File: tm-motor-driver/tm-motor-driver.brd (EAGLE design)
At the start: 50 x 27 mm, 18 parts

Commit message: Generate gerber files
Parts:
- moved C1 2.12 mm to (23.5, 12.5)
- moved C2 2.12 mm to (26.9, 16.5)
- moved D_0 2.12 mm to (33.5, 17.5)
- moved D_1 2.12 mm to (13.5, 17.5)
- moved LED_0 2.12 mm to (30.5, 17.5)
- moved LED_1 2.12 mm to (16.5, 17.5)
- moved MOSFET_0 2.12 mm to (34.5, 12.5)
- moved MOSFET_1 2.12 mm to (12.5, 12.5)
- moved MOTOR_0 2.12 mm to (41.5, 16.5)
- moved MOTOR_1 2.12 mm to (5.50, 16.5)
- moved POWER 2.12 mm to (17.5, 5.50)
- moved PWM 2.12 mm to (29.5, 5.50)
- moved R1 2.12 mm to (29.5, 12.5)
- moved R2 2.12 mm to (30.5, 22.5)
- moved R3 2.12 mm to (17.5, 12.5)
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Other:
- board size 50 x 27 mm -> 47 x 26 mm

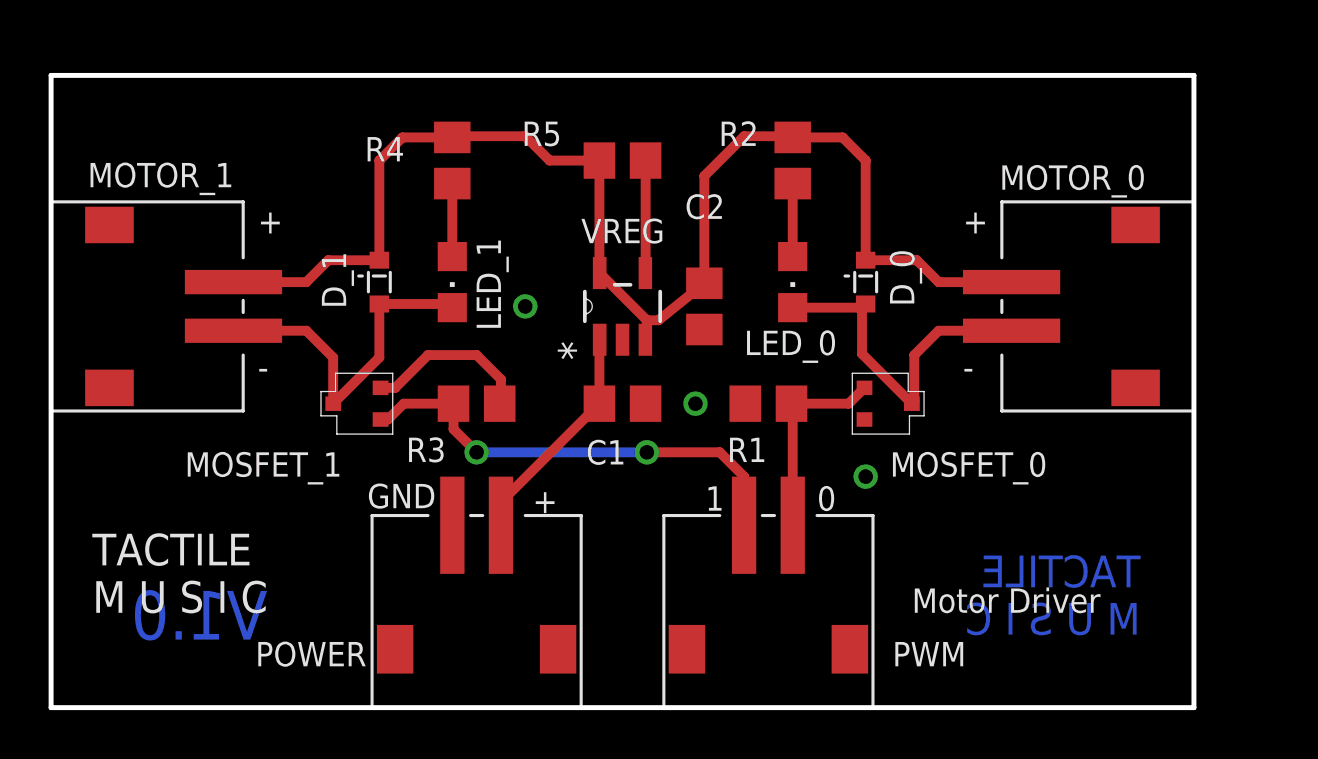
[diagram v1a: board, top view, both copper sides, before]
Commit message: Replaced JST with picoblade
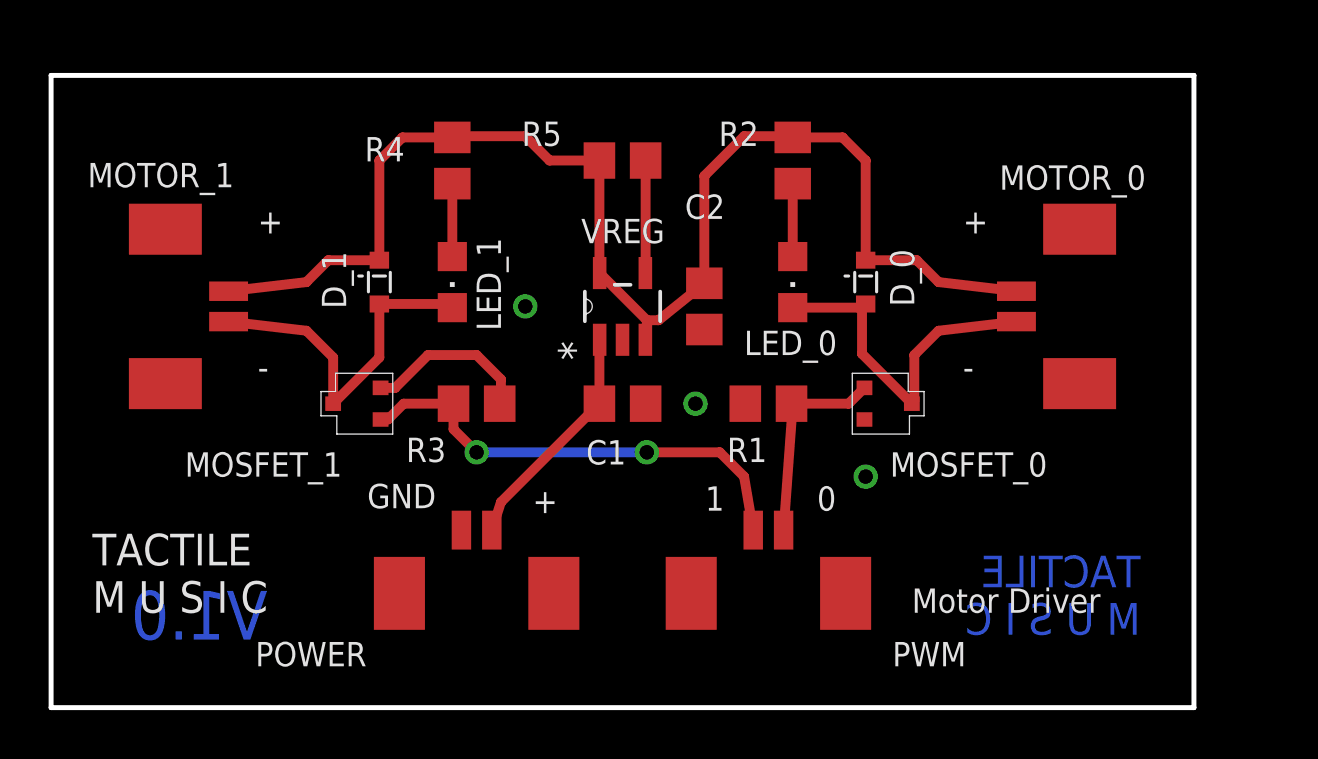
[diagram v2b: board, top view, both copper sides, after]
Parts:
- MOTOR_0, MOTOR_1, POWER, PWM: value JST-SMD-2 -> PICOBLADE; device tactile-music:JST-SMD-2 -> tactile-music:PICOBLADE
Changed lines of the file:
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@@
 <attribute name="NAME" x="34.5" y="9.5" size="1" layer="25" font="vector" ratio="20"/>
 </element>
-<element name="MOTOR_0" library="tactile-music" package="JST-SMD-2" value="JST-SMD-2" x="41.5" y="16.5" smashed="yes" rot="R90">
+<element name="MOTOR_0" library="tactile-music" package="PICOBLADE" value="PICOBLADE" x="41.5" y="16.5" smashed="yes" rot="R90">
 <attribute name="NAME" x="39" y="21.3" size="1" layer="25" font="vector" ratio="20"/>
 </element>
@@
 <attribute name="NAME" x="5.5" y="9.5" size="1" layer="25" font="vector" ratio="20"/>
 </element>
-<element name="MOTOR_1" library="tactile-music" package="JST-SMD-2" value="JST-SMD-2" x="5.5" y="16.5" smashed="yes" rot="R270">
+<element name="MOTOR_1" library="tactile-music" package="PICOBLADE" value="PICOBLADE" x="5.5" y="16.5" smashed="yes" rot="R270">
 <attribute name="NAME" x="1.5" y="21.4" size="1" layer="25" font="vector" ratio="20"/>
 </element>
@@
 <attribute name="VALUE" x="21.32" y="22.56" size="1" layer="27" font="vector" ratio="20" rot="R180"/>
 </element>
-<element name="POWER" library="tactile-music" package="JST-SMD-2" value="JST-SMD-2" x="17.5" y="5.5" smashed="yes">
+<element name="POWER" library="tactile-music" package="PICOBLADE" value="PICOBLADE" x="17.5" y="5.5" smashed="yes">
 <attribute name="NAME" x="8.4" y="1.7" size="1" layer="25" font="vector" ratio="20"/>
 </element>
-<element name="PWM" library="tactile-music" package="JST-SMD-2" value="JST-SMD-2" x="29.5" y="5.5" smashed="yes">
+<element name="PWM" library="tactile-music" package="PICOBLADE" value="PICOBLADE" x="29.5" y="5.5" smashed="yes">
 <attribute name="NAME" x="34.6" y="1.7" size="1" layer="25" font="vector" ratio="20"/>
 </element>
@@
 <wire x1="22.5602" y1="15.1284" x2="22.55" y2="15.1284" width="0.4064" layer="1"/>
 <wire x1="22.55" y1="15.1284" x2="22.55" y2="12.5" width="0.4064" layer="1"/>
-<wire x1="18.5" y1="7.5" x2="18.5" y2="8.45" width="0.4064" layer="1"/>
+<wire x1="18.125" y1="7.3" x2="18.5" y2="8.45" width="0.4064" layer="1"/>
 <wire x1="18.5" y1="8.45" x2="22.55" y2="12.5" width="0.4064" layer="1"/>
 </signal>
@@
 <contactref element="R1" pad="2"/>
 <contactref element="PWM" pad="2"/>
-<wire x1="30.5" y1="7.5" x2="30.5" y2="12.45" width="0.4064" layer="1"/>
+<wire x1="30.125" y1="7.3" x2="30.5" y2="12.45" width="0.4064" layer="1"/>
 <wire x1="30.5" y1="12.45" x2="30.45" y2="12.5" width="0.4064" layer="1"/>
 <wire x1="30.45" y1="12.5" x2="32.8" y2="12.5" width="0.4064" layer="1"/>
@@
 <wire x1="24.5" y1="10.5" x2="27.5" y2="10.5" width="0.4064" layer="1"/>
 <wire x1="27.5" y1="10.5" x2="28.5" y2="9.5" width="0.4064" layer="1"/>
-<wire x1="28.5" y1="9.5" x2="28.5" y2="7.5" width="0.4064" layer="1"/>
+<wire x1="28.5" y1="9.5" x2="28.875" y2="7.3" width="0.4064" layer="1"/>
 </signal>
 <signal name="GND">
@@
 <wire x1="13.5" y1="18.4" x2="11.4" y2="18.4" width="0.4064" layer="1"/>
 <wire x1="11.4" y1="18.4" x2="10.5" y2="17.5" width="0.4064" layer="1"/>
-<wire x1="10.5" y1="17.5" x2="7.5" y2="17.5" width="0.4064" layer="1"/>
+<wire x1="10.5" y1="17.5" x2="7.3" y2="17.125" width="0.4064" layer="1"/>
 <wire x1="22.5602" y1="17.8716" x2="22.5602" y2="17.4398" width="0.4064" layer="1"/>
 <wire x1="24.5" y1="15.1886" x2="24.4398" y2="15.1284" width="0.4064" layer="1"/>
@@
 <wire x1="33.5" y1="18.4" x2="35.6" y2="18.4" width="0.4064" layer="1"/>
 <wire x1="35.6" y1="18.4" x2="36.5" y2="17.5" width="0.4064" layer="1"/>
-<wire x1="36.5" y1="17.5" x2="39.5" y2="17.5" width="0.4064" layer="1"/>
+<wire x1="36.5" y1="17.5" x2="39.7" y2="17.125" width="0.4064" layer="1"/>
 <wire x1="24.5" y1="15.9318" x2="24.9818" y2="15.9318" width="0.4064" layer="1"/>
 <wire x1="24.9818" y1="15.9318" x2="26.865" y2="17.45" width="0.4064" layer="1"/>
@@
 <wire x1="33.35" y1="16.45" x2="33.35" y2="14.55" width="0.4064" layer="1"/>
 <wire x1="33.35" y1="14.55" x2="35.4" y2="12.5" width="0.4064" layer="1"/>
-<wire x1="39.5" y1="15.5" x2="36.5" y2="15.5" width="0.4064" layer="1"/>
+<wire x1="39.7" y1="15.875" x2="36.5" y2="15.5" width="0.4064" layer="1"/>
 <wire x1="36.5" y1="15.5" x2="35.5" y2="14.5" width="0.4064" layer="1"/>
 <wire x1="35.5" y1="14.5" x2="35.5" y2="12.6" width="0.4064" layer="1"/>
@@
 <wire x1="11.6" y1="12.5" x2="11.6" y2="14.4" width="0.4064" layer="1"/>
 <wire x1="11.6" y1="14.4" x2="10.5" y2="15.5" width="0.4064" layer="1"/>
-<wire x1="10.5" y1="15.5" x2="7.5" y2="15.5" width="0.4064" layer="1"/>
+<wire x1="10.5" y1="15.5" x2="7.3" y2="15.875" width="0.4064" layer="1"/>
 </signal>
 <signal name="N$7">
